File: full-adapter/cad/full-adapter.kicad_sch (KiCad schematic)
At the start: 0 parts

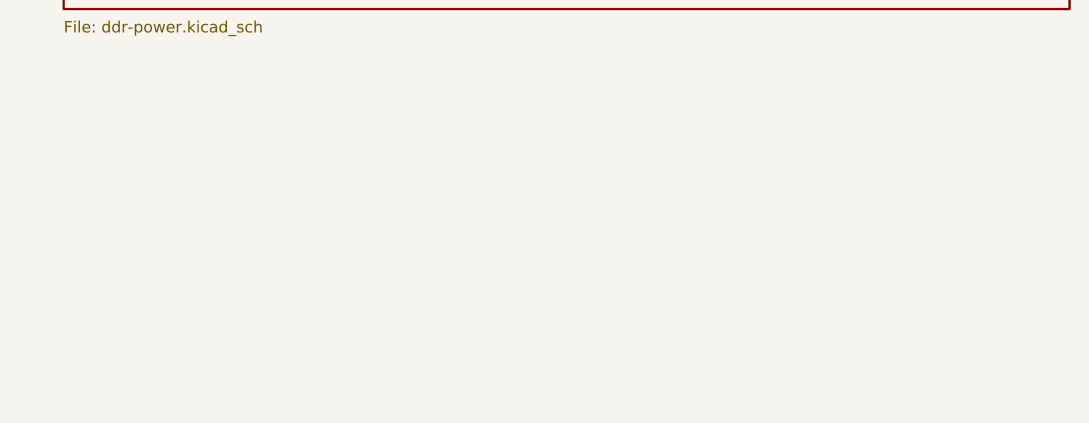
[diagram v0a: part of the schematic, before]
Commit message: cad: capture processor core bypass and all 208 ground balls
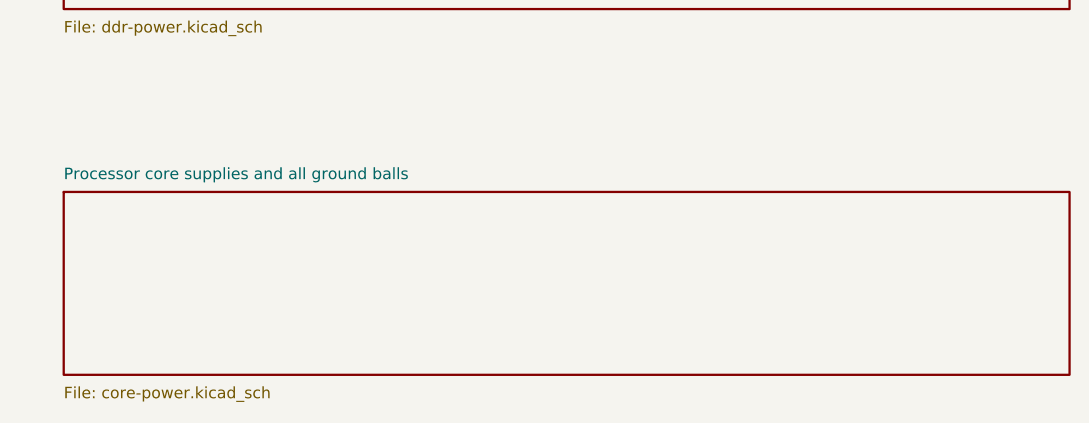
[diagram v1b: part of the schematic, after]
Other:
- added sheet Processor core supplies and all ground balls (core-power.kicad_sch)
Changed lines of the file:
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@@
 (sheet (at 25.4 76.2) (size 111.76 20.32) (fields_autoplaced yes) (stroke (width 0.254) (type default)) (fill (color 0 0 0 0)) (property "Sheetname" "1 GiB DDR3: command, data and clock termination" (at 25.4 74.93 0) (effects (font (size 1.27 1.27)) (justify left bottom))) (property "Sheetfile" "ddr-signals.kicad_sch" (at 25.4 97.79 0) (effects (font (size 1.27 1.27)) (justify left top))))
 (sheet (at 25.4 116.84) (size 111.76 20.32) (fields_autoplaced yes) (stroke (width 0.254) (type default)) (fill (color 0 0 0 0)) (property "Sheetname" "DDR3 references, calibration and local bypass" (at 25.4 115.57000000000001 0) (effects (font (size 1.27 1.27)) (justify left bottom))) (property "Sheetfile" "ddr-power.kicad_sch" (at 25.4 138.43 0) (effects (font (size 1.27 1.27)) (justify left top))))
+(sheet (at 25.4 157.48000000000002) (size 111.76 20.32) (fields_autoplaced yes) (stroke (width 0.254) (type default)) (fill (color 0 0 0 0)) (property "Sheetname" "Processor core supplies and all ground balls" (at 25.4 156.21 0) (effects (font (size 1.27 1.27)) (justify left bottom))) (property "Sheetfile" "core-power.kicad_sch" (at 25.4 179.07000000000002 0) (effects (font (size 1.27 1.27)) (justify left top))))
 )

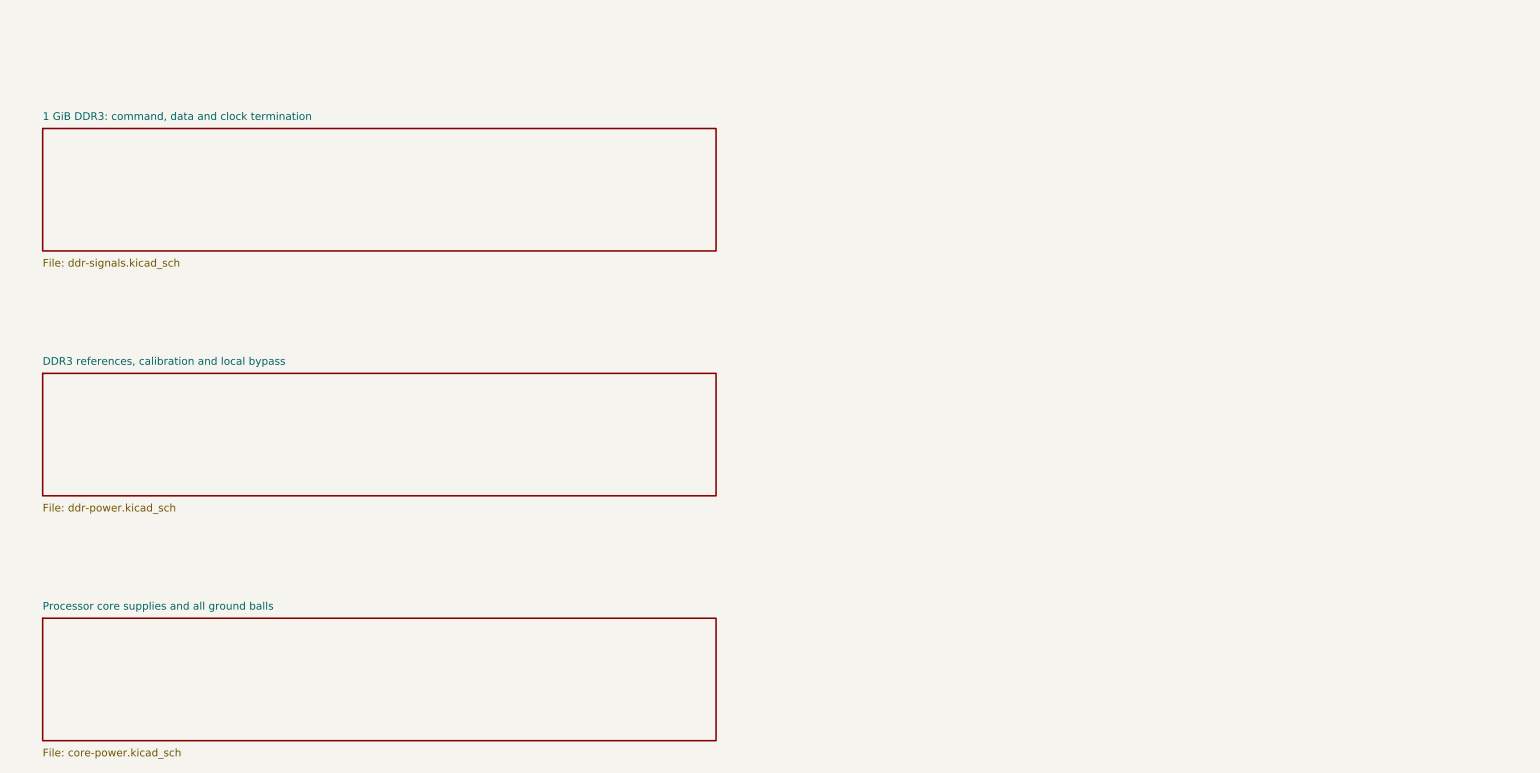
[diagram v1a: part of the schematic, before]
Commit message: cad: capture CPU buck regulator with remote sense and hardware defaults
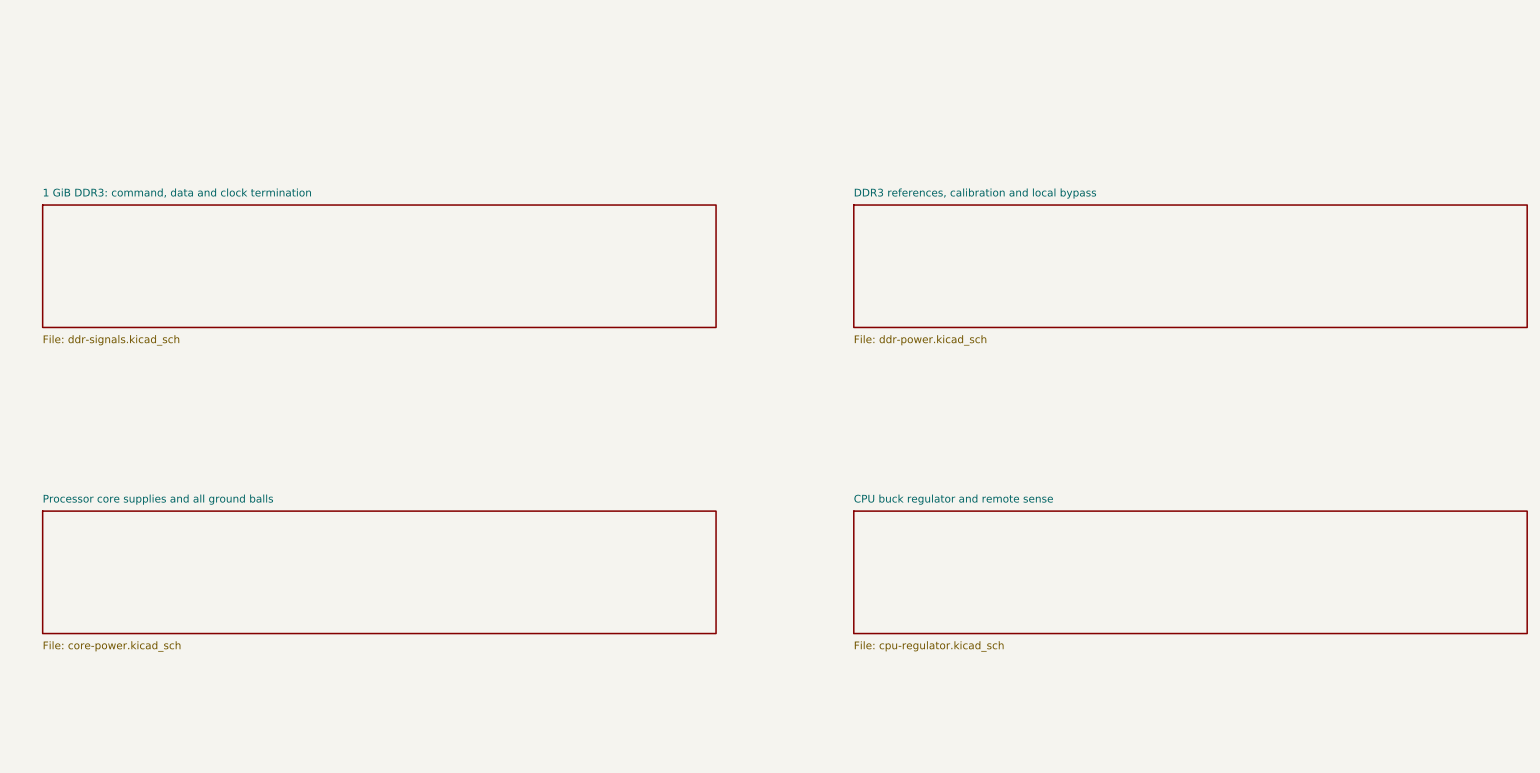
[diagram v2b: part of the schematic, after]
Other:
- added sheet CPU buck regulator and remote sense (cpu-regulator.kicad_sch)
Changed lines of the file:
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@@
 (text "CURRENT DESIGN — IN PROGRESS" (at 20.32 20.32 0) (effects (font (size 2.54 2.54)) (justify left top)))
 (text "RK3568B2 + 1 GiB DDR3 + PCIe RTL8125BG-CG\nUSB3 M.2 modem; isolated PoE and USB-C auxiliary power\n\nDDR capture is present. Remaining subsystem capture and PCB routing\nare active work. This project is not a manufacturing release." (at 20.32 33.02 0) (effects (font (size 1.8 1.8)) (justify left top)))
-(sheet (at 25.4 76.2) (size 111.76 20.32) (fields_autoplaced yes) (stroke (width 0.254) (type default)) (fill (color 0 0 0 0)) (property "Sheetname" "1 GiB DDR3: command, data and clock termination" (at 25.4 74.93 0) (effects (font (size 1.27 1.27)) (justify left bottom))) (property "Sheetfile" "ddr-signals.kicad_sch" (at 25.4 97.79 0) (effects (font (size 1.27 1.27)) (justify left top))))
-(sheet (at 25.4 116.84) (size 111.76 20.32) (fields_autoplaced yes) (stroke (width 0.254) (type default)) (fill (color 0 0 0 0)) (property "Sheetname" "DDR3 references, calibration and local bypass" (at 25.4 115.57000000000001 0) (effects (font (size 1.27 1.27)) (justify left bottom))) (property "Sheetfile" "ddr-power.kicad_sch" (at 25.4 138.43 0) (effects (font (size 1.27 1.27)) (justify left top))))
-(sheet (at 25.4 157.48000000000002) (size 111.76 20.32) (fields_autoplaced yes) (stroke (width 0.254) (type default)) (fill (color 0 0 0 0)) (property "Sheetname" "Processor core supplies and all ground balls" (at 25.4 156.21 0) (effects (font (size 1.27 1.27)) (justify left bottom))) (property "Sheetfile" "core-power.kicad_sch" (at 25.4 179.07000000000002 0) (effects (font (size 1.27 1.27)) (justify left top))))
+(sheet (at 25.4 88.9) (size 111.76 20.32) (fields_autoplaced yes) (stroke (width 0.254) (type default)) (fill (color 0 0 0 0)) (property "Sheetname" "1 GiB DDR3: command, data and clock termination" (at 25.4 87.63000000000001 0) (effects (font (size 1.27 1.27)) (justify left bottom))) (property "Sheetfile" "ddr-signals.kicad_sch" (at 25.4 110.49000000000001 0) (effects (font (size 1.27 1.27)) (justify left top))))
+(sheet (at 160.02 88.9) (size 111.76 20.32) (fields_autoplaced yes) (stroke (width 0.254) (type default)) (fill (color 0 0 0 0)) (property "Sheetname" "DDR3 references, calibration and local bypass" (at 160.02 87.63000000000001 0) (effects (font (size 1.27 1.27)) (justify left bottom))) (property "Sheetfile" "ddr-power.kicad_sch" (at 160.02 110.49000000000001 0) (effects (font (size 1.27 1.27)) (justify left top))))
+(sheet (at 25.4 139.7) (size 111.76 20.32) (fields_autoplaced yes) (stroke (width 0.254) (type default)) (fill (color 0 0 0 0)) (property "Sheetname" "Processor core supplies and all ground balls" (at 25.4 138.42999999999998 0) (effects (font (size 1.27 1.27)) (justify left bottom))) (property "Sheetfile" "core-power.kicad_sch" (at 25.4 161.29 0) (effects (font (size 1.27 1.27)) (justify left top))))
+(sheet (at 160.02 139.7) (size 111.76 20.32) (fields_autoplaced yes) (stroke (width 0.254) (type default)) (fill (color 0 0 0 0)) (property "Sheetname" "CPU buck regulator and remote sense" (at 160.02 138.42999999999998 0) (effects (font (size 1.27 1.27)) (justify left bottom))) (property "Sheetfile" "cpu-regulator.kicad_sch" (at 160.02 161.29 0) (effects (font (size 1.27 1.27)) (justify left top))))
 )

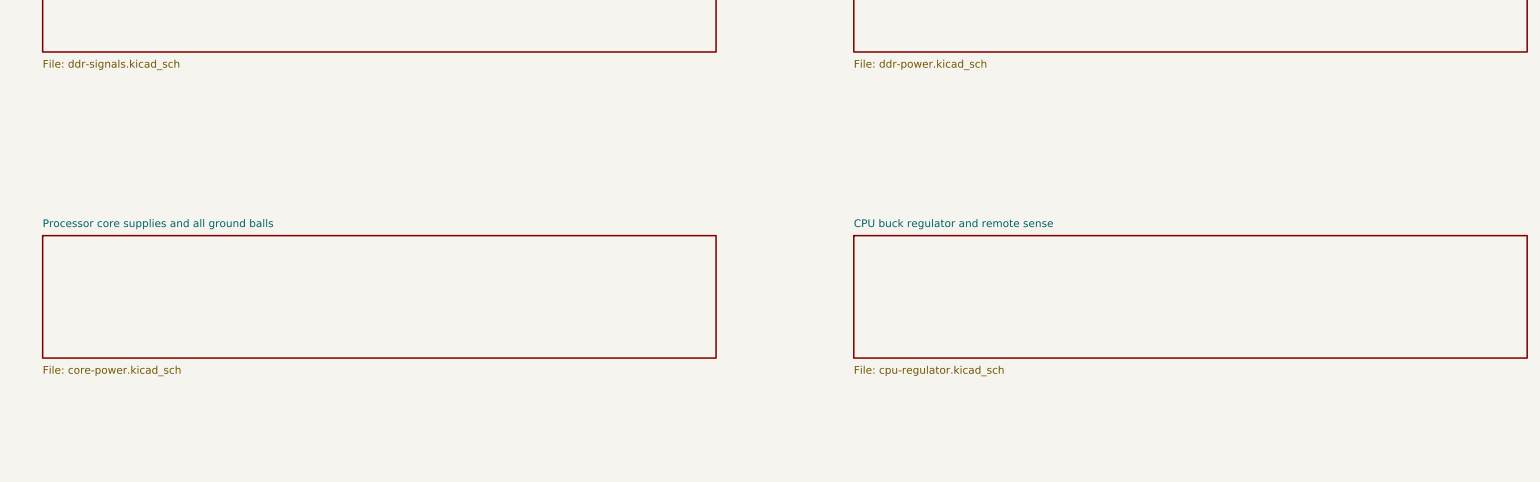
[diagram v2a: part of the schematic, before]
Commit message: Capture RK809 LDO supplies and CPU enable source
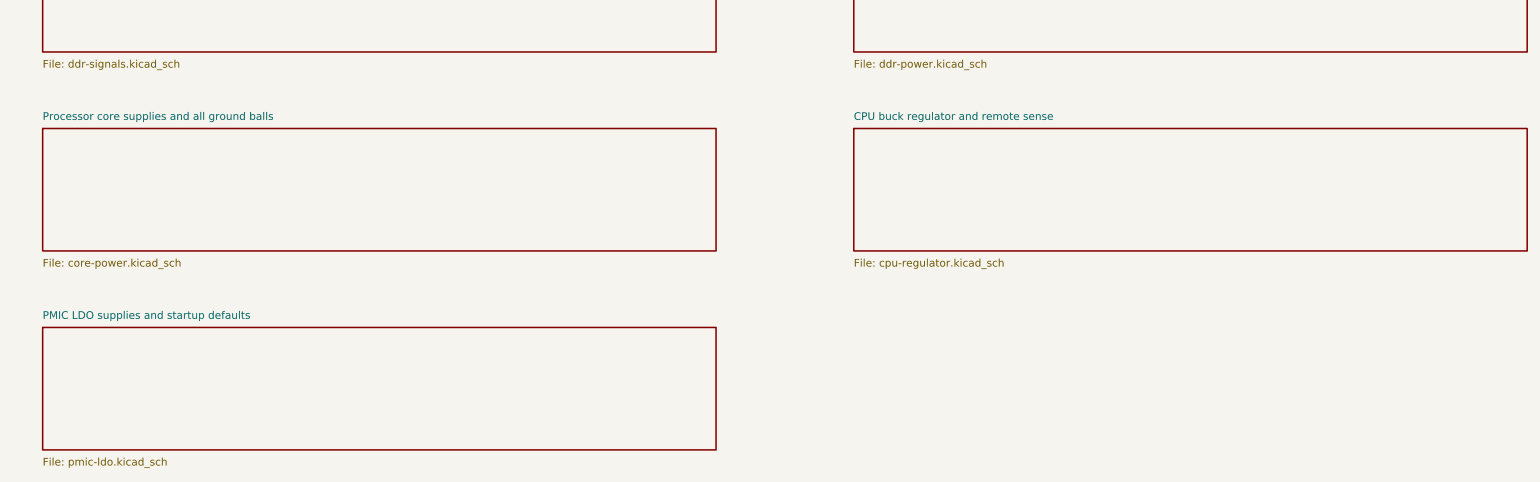
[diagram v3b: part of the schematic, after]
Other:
- added sheet PMIC LDO supplies and startup defaults (pmic-ldo.kicad_sch)
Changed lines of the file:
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@@
 (sheet (at 25.4 88.9) (size 111.76 20.32) (fields_autoplaced yes) (stroke (width 0.254) (type default)) (fill (color 0 0 0 0)) (property "Sheetname" "1 GiB DDR3: command, data and clock termination" (at 25.4 87.63000000000001 0) (effects (font (size 1.27 1.27)) (justify left bottom))) (property "Sheetfile" "ddr-signals.kicad_sch" (at 25.4 110.49000000000001 0) (effects (font (size 1.27 1.27)) (justify left top))))
 (sheet (at 160.02 88.9) (size 111.76 20.32) (fields_autoplaced yes) (stroke (width 0.254) (type default)) (fill (color 0 0 0 0)) (property "Sheetname" "DDR3 references, calibration and local bypass" (at 160.02 87.63000000000001 0) (effects (font (size 1.27 1.27)) (justify left bottom))) (property "Sheetfile" "ddr-power.kicad_sch" (at 160.02 110.49000000000001 0) (effects (font (size 1.27 1.27)) (justify left top))))
-(sheet (at 25.4 139.7) (size 111.76 20.32) (fields_autoplaced yes) (stroke (width 0.254) (type default)) (fill (color 0 0 0 0)) (property "Sheetname" "Processor core supplies and all ground balls" (at 25.4 138.42999999999998 0) (effects (font (size 1.27 1.27)) (justify left bottom))) (property "Sheetfile" "core-power.kicad_sch" (at 25.4 161.29 0) (effects (font (size 1.27 1.27)) (justify left top))))
-(sheet (at 160.02 139.7) (size 111.76 20.32) (fields_autoplaced yes) (stroke (width 0.254) (type default)) (fill (color 0 0 0 0)) (property "Sheetname" "CPU buck regulator and remote sense" (at 160.02 138.42999999999998 0) (effects (font (size 1.27 1.27)) (justify left bottom))) (property "Sheetfile" "cpu-regulator.kicad_sch" (at 160.02 161.29 0) (effects (font (size 1.27 1.27)) (justify left top))))
+(sheet (at 25.4 121.92000000000002) (size 111.76 20.32) (fields_autoplaced yes) (stroke (width 0.254) (type default)) (fill (color 0 0 0 0)) (property "Sheetname" "Processor core supplies and all ground balls" (at 25.4 120.65000000000002 0) (effects (font (size 1.27 1.27)) (justify left bottom))) (property "Sheetfile" "core-power.kicad_sch" (at 25.4 143.51000000000002 0) (effects (font (size 1.27 1.27)) (justify left top))))
+(sheet (at 160.02 121.92000000000002) (size 111.76 20.32) (fields_autoplaced yes) (stroke (width 0.254) (type default)) (fill (color 0 0 0 0)) (property "Sheetname" "CPU buck regulator and remote sense" (at 160.02 120.65000000000002 0) (effects (font (size 1.27 1.27)) (justify left bottom))) (property "Sheetfile" "cpu-regulator.kicad_sch" (at 160.02 143.51000000000002 0) (effects (font (size 1.27 1.27)) (justify left top))))
+(sheet (at 25.4 154.94) (size 111.76 20.32) (fields_autoplaced yes) (stroke (width 0.254) (type default)) (fill (color 0 0 0 0)) (property "Sheetname" "PMIC LDO supplies and startup defaults" (at 25.4 153.67 0) (effects (font (size 1.27 1.27)) (justify left bottom))) (property "Sheetfile" "pmic-ldo.kicad_sch" (at 25.4 176.53 0) (effects (font (size 1.27 1.27)) (justify left top))))
 )
